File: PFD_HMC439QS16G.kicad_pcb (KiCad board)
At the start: 2 copper layers, 60.5 x 40.4 mm, 47 parts, among them J1 REF, J2 IN, J3 Out, J4 Supply, U1 HMC439QS16G, U2 LT3045EMSE, U3 LT3094EMSE, U4 ADA4896-2ARMZ

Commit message: Rev 1.1
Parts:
- removed REF** (x4): MountingHole_2.7mm_M2.5, Mounting_Holes:MountingHole_2.7mm_M2.5
- removed REF***: OSHW-Logo_5.7x6mm_SilkScreen, Symbols:OSHW-Logo_5.7x6mm_SilkScreen
- added C20: 560p, Capacitor_SMD:C_0603_1608Metric, F.Cu at (152.2, 100.8)
- added C21: 100n, Capacitor_SMD:C_0603_1608Metric, F.Cu at (136.8, 108.8)
- added C22: 100n, Capacitor_SMD:C_0603_1608Metric, F.Cu at (129.8, 114.8)
- added C23: 33p, Capacitor_SMD:C_0603_1608Metric, F.Cu at (125.2, 110.8)
- added C24: 330p, Capacitor_SMD:C_0603_1608Metric, F.Cu at (119.4, 106.1)
- added H1: MountingHole_Pad, MountingHole:MountingHole_4.3mm_M4_Pad_Via, F.Cu at (109.4, 73.5)
- added H2: MountingHole_Pad, MountingHole:MountingHole_4.3mm_M4_Pad_Via, F.Cu at (187.7, 73.5)
- added H3: MountingHole_Pad, MountingHole:MountingHole_4.3mm_M4_Pad_Via, F.Cu at (187.4, 121.6)
- added H4: MountingHole_Pad, MountingHole:MountingHole_4.3mm_M4_Pad_Via, F.Cu at (109.4, 121.5)
- added J5: JFET/Bias-T, Connector_Coaxial:SMA_Amphenol_901-144_Vertical, F.Cu at (111.8, 106.9)
- added JP1: Inverting, Jumper:SolderJumper-2_P1.3mm_Open_RoundedPad1.0x1.5mm, F.Cu at (129.9, 107.0)
- added JP2: Non-Inverting, Jumper:SolderJumper-2_P1.3mm_Open_RoundedPad1.0x1.5mm, F.Cu at (123.0, 109.5)
- added LOGO1: Logo_APQ, footprints:APQ-Logo, F.Cu at (143.0, 72.8)
- added LOGO2: Logo_Open_Hardware_Small, Symbol:OSHW-Logo_5.7x6mm_SilkScreen, B.Cu at (152.0, 118.8)
- added LOGO3: Logo_ROHS, Symbol:RoHS-Logo_6mm_SilkScreen, B.Cu at (169.0, 119.2)
- added R16: 200, Resistor_SMD:R_0603_1608Metric, F.Cu at (145.8, 121.0)
- added R17: 200, Resistor_SMD:R_0603_1608Metric, F.Cu at (134.0, 114.2)
- added R18: 200, Resistor_SMD:R_0603_1608Metric, F.Cu at (127.5, 110.8)
- added R19: 51, Resistor_SMD:R_1210_3225Metric, F.Cu at (126.2, 105.5)
- added R20: 1.2k, Resistor_SMD:R_0603_1608Metric, F.Cu at (122.1, 106.9)
- added R21: 51, Resistor_SMD:R_0603_1608Metric, F.Cu at (117.5, 106.1)
- added RV1: 1k, Potentiometer_THT:Potentiometer_Vishay_43_Horizontal, F.Cu at (142.2, 108.2)
- added U5: ADA4896-2ARMZ, footprints:MSOP-8_3x3mm_P0.65mm_mod, F.Cu at (132.2, 111.0)
- C1, C2: footprint Capacitors_SMD:C_0402 -> Capacitor_SMD:C_0402_1005Metric
- C10, C15, C16, C17, C18, C19, C5, C6, C9: footprint Capacitors_SMD:C_0603 -> Capacitor_SMD:C_0603_1608Metric
- C11, C12, C3, C4: footprint Capacitors_SMD:C_1210 -> Capacitor_SMD:C_1210_3225Metric
- C13, C14: value 200p -> 33p; footprint Capacitors_SMD:C_0603 -> Capacitor_SMD:C_0603_1608Metric
- C7: footprint Capacitors_SMD:C_1206 -> Capacitor_SMD:C_1206_3216Metric
- C8: value 4.7u -> 0.47u; footprint Capacitors_SMD:C_1206 -> Capacitor_SMD:C_1206_3216Metric
- J1, J2: footprint Connectors:SMA_THT_Jack_Straight -> Connector_Coaxial:SMA_Amphenol_901-144_Vertical
- J3: value Out -> Error_Out; footprint Connectors:SMA_THT_Jack_Straight -> Connector_Coaxial:SMA_Amphenol_901-144_Vertical
- J4: footprint Pin_Headers:Pin_Header_Straight_1x03_Pitch2.54mm -> Connector_PinHeader_2.54mm:PinHeader_1x03_P2.54mm_Vertical
- R1, R10, R11, R12, R13, R14, R2, R3, R4, R5, R6, R7, R8, R9: footprint Resistors_SMD:R_0603 -> Resistor_SMD:R_0603_1608Metric
- R15: footprint Resistors_SMD:R_1210 -> Resistor_SMD:R_1210_3225Metric
- U1: footprint custom:QSOP-16_EP_3.9x4.9mm_Pitch0.635mm -> footprints:QSOP-16_3.9x4.9mm_P0.635mm_EP_2.3mmx1.75mm
- U2, U3: footprint Housings_SSOP:MSOP-12-1EP_3x4mm_Pitch0.65mm -> Package_SO:MSOP-12-1EP_3x4mm_P0.65mm_EP1.65x2.85mm
- U4: footprint Housings_SSOP:MSOP-8_3x3mm_Pitch0.65mm -> footprints:MSOP-8_3x3mm_P0.65mm_mod
- moved C1 48.6 mm to (182.3, 106.9)
- moved J1 48.6 mm to (188.2, 106.9)
- moved C2 46.8 mm to (182.5, 91.8)
- moved J2 46.8 mm to (188.2, 91.8)
- moved R13 46.0 mm to (141.2, 98.8)
- moved C19 46.0 mm to (162.8, 106.4)
- moved C14 45.8 mm to (157.2, 94.7)
- moved C5 45.8 mm to (175.5, 100.0)
- moved C6 45.8 mm to (174.5, 95.4)
- moved R5 45.8 mm to (159.9, 96.3)
- moved R8 45.8 mm to (156.4, 102.4)
- moved U1 45.8 mm to (170.0, 99.7)
- moved C13 45.8 mm to (157.1, 104.8)
- moved R3 45.8 mm to (165.2, 94.2)
- moved R4 45.8 mm to (162.8, 103.2)
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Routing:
- net GND: track 254.2 -> 72.4 mm, vias 176 -> 237
- net IN: track 48.5 -> 14.5 mm, vias 9 -> 12
- net +5V: track 108.4 -> 140.9 mm
- net Net-(C16-Pad1): track 8.48 -> 36.4 mm, vias 0 -> 2
- net -5V: track 25.3 -> 43.9 mm
- net Net-(JP1-Pad1): track 0.00 -> 12.0 mm
- net Net-(C23-Pad2): track 0.00 -> 10.9 mm
- net Net-(C20-Pad1): track 10.0 -> 19.9 mm
- net Net-(C24-Pad1): track 0.00 -> 9.49 mm
- net Net-(RV1-Pad2): track 0.00 -> 8.91 mm
- net Net-(JP1-Pad2): track 0.00 -> 8.57 mm
- net Net-(C23-Pad1): track 0.00 -> 8.36 mm
- net Net-(C15-Pad1): track 6.74 -> 10.2 mm
- net Net-(C2-Pad1): track 8.97 -> 12.2 mm
- net Net-(C1-Pad1): track 8.82 -> 11.8 mm
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- added copper zone on B.Cu, net IN
- added copper zone on F.Cu, net IN
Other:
- board size 60.5 x 40.4 mm -> 108 x 58 mm
- board text added: "GND"
- board text added: "JFET/Bias-T non-inverting: JP1:open, JP2:closed, R17=R18 JFET/Bias-T inverting: JP1:closed, JP2:open, R17:DNF"
- board text added: "Phase-Frequency Detector 11/2020 Rev 1.1 Design: Tilman Preuschoff"
- board text removed: "Design: Tilman Preuschoff"
- board text removed: "Phase Frequency Detector 2019/02 Rev. 1.0"

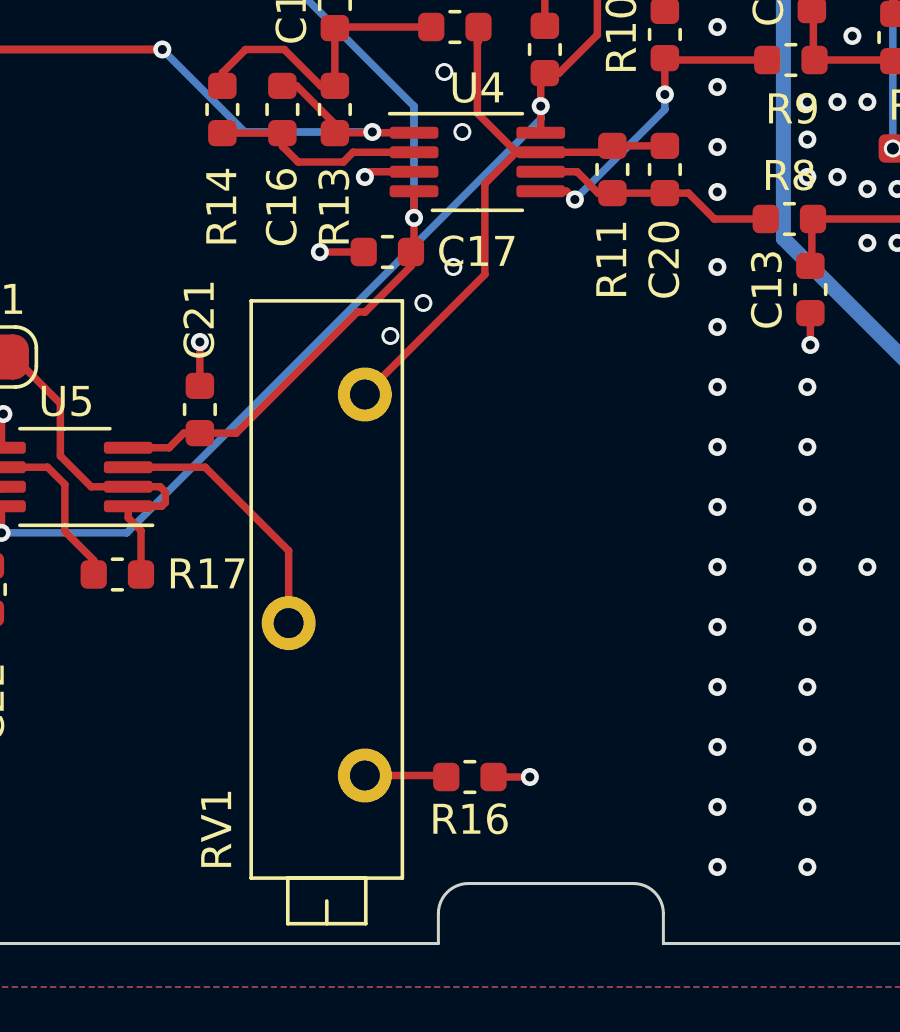
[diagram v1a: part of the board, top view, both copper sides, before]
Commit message: Reverse Trimpot. Update gerber files
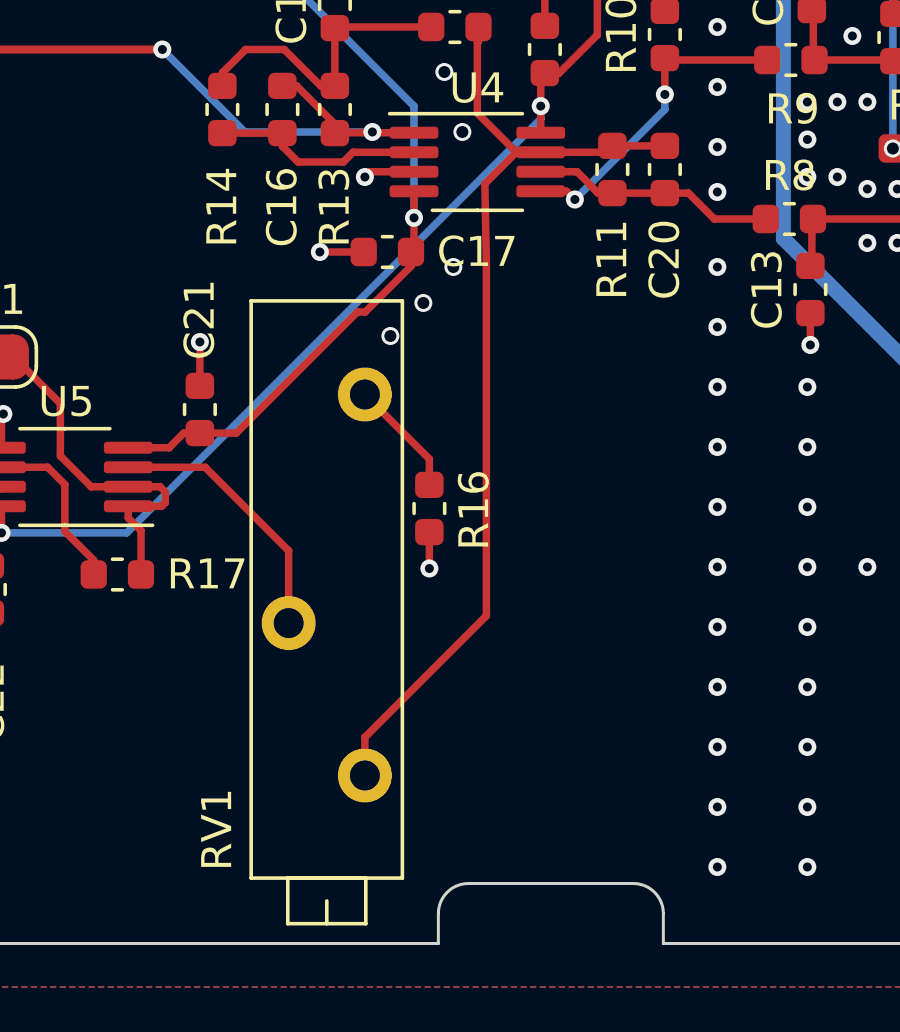
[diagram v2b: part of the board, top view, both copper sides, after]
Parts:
- moved R16 9.05 mm to (144.4, 112.0), turned to 90 degrees
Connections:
- RV1 pad 1: Net-(C20-Pad1) -> Net-(R16-Pad2)
- RV1 pad 3: Net-(R16-Pad2) -> Net-(C20-Pad1)
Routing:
- net Net-(C20-Pad1): track 19.9 -> 32.7 mm
- net Net-(R16-Pad2): track 2.73 -> 3.97 mm
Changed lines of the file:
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@@
     (thickness 1.6)
     (drawings 136)
-    (tracks 625)
+    (tracks 628)
     (zones 0)
     (modules 65)
@@
   )
   (module Resistor_SMD:R_0603_1608Metric (layer F.Cu)
-    (at 145.75 121 180)
+    (at 144.4 112.05 90)
     (descr "Resistor SMD 0603 (1608 Metric), square (rectangular) end terminal, IPC_7351 nominal, (Body size source: http://www.tortai-tech.com/upload/download/2011102023233369053.pdf), generated with kicad-footprint-generator")
     (tags resistor)
     (attr smd)
-    (fp_text reference R16 (at 0 -1.43) (layer F.SilkS)
+    (fp_text reference R16 (at -0.05 1.5 90) (layer F.SilkS)
       (effects (font (size 1 1) (thickness 0.15)))
     )
-    (fp_text value 200 (at 0 1.43) (layer F.Fab)
+    (fp_text value 200 (at 0 1.43 90) (layer F.Fab)
       (effects (font (size 1 1) (thickness 0.15)))
     )
@@
     (fp_line (start 1.48 -0.73) (end 1.48 0.73) (layer F.CrtYd) (width 0.05))
     (fp_line (start 1.48 0.73) (end -1.48 0.73) (layer F.CrtYd) (width 0.05))
-    (fp_text user %R (at 0 0) (layer F.Fab)
+    (fp_text user %R (at 0 0 90) (layer F.Fab)
       (effects (font (size 0.4 0.4) (thickness 0.06)))
     )
-    (pad 1 smd roundrect (at -0.7875 0 180) (size 0.875 0.95) (layers F.Cu F.Paste F.Mask) (roundrect_rratio 0.25)
+    (pad 1 smd roundrect (at -0.7875 0 90) (size 0.875 0.95) (layers F.Cu F.Paste F.Mask) (roundrect_rratio 0.25)
       (net 5 GND))
-    (pad 2 smd roundrect (at 0.7875 0 180) (size 0.875 0.95) (layers F.Cu F.Paste F.Mask) (roundrect_rratio 0.25)
+    (pad 2 smd roundrect (at 0.7875 0 90) (size 0.875 0.95) (layers F.Cu F.Paste F.Mask) (roundrect_rratio 0.25)
       (net 36 "Net-(R16-Pad2)"))
     (model ${KISYS3DMOD}/Resistor_SMD.3dshapes/R_0603_1608Metric.wrl
@@
     )
     (pad 1 thru_hole circle (at 0 0 90) (size 1.8 1.8) (drill 1) (layers *.Cu *.Mask)
-      (net 28 "Net-(C20-Pad1)"))
+      (net 36 "Net-(R16-Pad2)"))
     (pad 2 thru_hole circle (at -7.62 -2.54 90) (size 1.8 1.8) (drill 1) (layers *.Cu *.Mask)
       (net 37 "Net-(RV1-Pad2)"))
     (pad 3 thru_hole circle (at -12.7 0 90) (size 1.8 1.8) (drill 1) (layers *.Cu *.Mask)
-      (net 36 "Net-(R16-Pad2)"))
+      (net 28 "Net-(C20-Pad1)"))
     (model ${KISYS3DMOD}/Potentiometer_THT.3dshapes/Potentiometer_Vishay_43_Horizontal.wrl
       (at (xyz 0 0 0))
@@
   (gr_line (start 122.4 69.55) (end 116.4 69.55) (layer Dwgs.User) (width 0.2))
   (dimension 108 (width 0.3) (layer Dwgs.User)
-    (gr_text "108,000 mm" (at 148.4 142.35) (layer Dwgs.User)
+    (gr_text "108,000 mm" (at 123.05 114.7 90) (layer Dwgs.User)
       (effects (font (size 1.5 1.5) (thickness 0.3)))
     )
-    (feature1 (pts (xy 94.4 113.55) (xy 94.4 140.836421)))
-    (feature2 (pts (xy 202.4 113.55) (xy 202.4 140.836421)))
-    (crossbar (pts (xy 202.4 140.25) (xy 94.4 140.25)))
-    (arrow1a (pts (xy 94.4 140.25) (xy 95.526504 139.663579)))
-    (arrow1b (pts (xy 94.4 140.25) (xy 95.526504 140.836421)))
-    (arrow2a (pts (xy 202.4 140.25) (xy 201.273496 139.663579)))
-    (arrow2b (pts (xy 202.4 140.25) (xy 201.273496 140.836421)))
+    (feature1 (pts (xy 151.85 60.7) (xy 124.563579 60.7)))
+    (feature2 (pts (xy 151.85 168.7) (xy 124.563579 168.7)))
+    (crossbar (pts (xy 125.15 168.7) (xy 125.15 60.7)))
+    (arrow1a (pts (xy 125.15 60.7) (xy 125.736421 61.826504)))
+    (arrow1b (pts (xy 125.15 60.7) (xy 124.563579 61.826504)))
+    (arrow2a (pts (xy 125.15 168.7) (xy 125.736421 167.573496)))
+    (arrow2b (pts (xy 125.15 168.7) (xy 124.563579 167.573496)))
   )
   (gr_line (start 116.4 69.55) (end 116.4 68.05) (layer Dwgs.User) (width 0.2))
@@
   (via (at 163 95.25) (size 0.6) (drill 0.3) (layers F.Cu B.Cu) (net 5))
   (via (at 164 95.25) (size 0.6) (drill 0.3) (layers F.Cu B.Cu) (net 5))
-  (via (at 147.75 121) (size 0.6) (drill 0.3) (layers F.Cu B.Cu) (net 5))
-  (segment (start 146.5375 121) (end 147.75 121) (width 0.25) (layer F.Cu) (net 5))
+  (via (at 144.4 114.05) (size 0.6) (drill 0.3) (layers F.Cu B.Cu) (net 5))
+  (segment (start 144.4 112.8375) (end 144.4 114.05) (width 0.25) (layer F.Cu) (net 5))
   (via (at 130.2 108.9) (size 0.6) (drill 0.3) (layers F.Cu B.Cu) (net 5))
   (segment (start 130.1375 110.025) (end 130.1375 108.9625) (width 0.25) (layer F.Cu) (net 5))
@@
   (segment (start 146.0375 96) (end 146.0375 96.475) (width 0.25) (layer F.Cu) (net 28))
   (segment (start 146.0375 96.475) (end 146 96.5125) (width 0.25) (layer F.Cu) (net 28))
-  (segment (start 142.25 108.25) (end 146.25 104.25) (width 0.25) (layer F.Cu) (net 28))
   (segment (start 147.3 100.175) (end 148.1125 100.175) (width 0.25) (layer F.Cu) (net 28))
   (segment (start 146.25 101.225) (end 147.3 100.175) (width 0.25) (layer F.Cu) (net 28))
-  (segment (start 146.25 104.25) (end 146.25 101.225) (width 0.25) (layer F.Cu) (net 28))
-  (segment (start 125.75 106.9) (end 125.85 107) (width 0.25) (layer F.Cu) (net 38))
-  (segment (start 122.8875 106.9) (end 125.75 106.9) (width 0.25) (layer F.Cu) (net 38))
+  (segment (start 146.3 115.627208) (end 146.3 103.9) (width 0.25) (layer F.Cu) (net 28))
+  (segment (start 142.25 119.677208) (end 146.3 115.627208) (width 0.25) (layer F.Cu) (net 28))
+  (segment (start 142.25 120.95) (end 142.25 119.677208) (width 0.25) (layer F.Cu) (net 28))
+  (segment (start 146.3 103.9) (end 146.25 101.225) (width 0.25) (layer F.Cu) (net 28))
   (segment (start 125.25 111.5375) (end 127.5 111.5375) (width 0.25) (layer F.Cu) (net 29))
   (segment (start 128.1875 111.325) (end 129.325 111.325) (width 0.25) (layer F.Cu) (net 29))
@@
   (segment (start 130.1375 111.325) (end 130.1375 111.3875) (width 0.25) (layer F.Cu) (net 29))
   (segment (start 130.1375 111.3875) (end 130.14999 111.39999) (width 0.25) (layer F.Cu) (net 29))
-  (segment (start 122.8875 107.375) (end 122.8875 106.9) (width 0.25) (layer F.Cu) (net 38))
   (segment (start 125.25 111.5375) (end 124.775 111.5375) (width 0.25) (layer F.Cu) (net 29))
   (segment (start 124.3875 111.5375) (end 125.25 111.5375) (width 0.25) (layer F.Cu) (net 29))
@@
   (segment (start 135.475 111.975) (end 134.3625 111.975) (width 0.25) (layer F.Cu) (net 35))
   (segment (start 135.425 111.325) (end 135.6 111.5) (width 0.25) (layer F.Cu) (net 35))
-  (segment (start 144.9125 120.95) (end 144.9625 121) (width 0.25) (layer F.Cu) (net 36))
-  (segment (start 142.25 120.95) (end 144.9125 120.95) (width 0.25) (layer F.Cu) (net 36))
+  (segment (start 144.45 111.2125) (end 144.4 111.2625) (width 0.25) (layer F.Cu) (net 36))
+  (segment (start 144.4 110.4) (end 144.4 111.2625) (width 0.25) (layer F.Cu) (net 36))
+  (segment (start 142.25 108.25) (end 144.4 110.4) (width 0.25) (layer F.Cu) (net 36))
   (segment (start 134.3625 110.675) (end 136.925 110.675) (width 0.25) (layer F.Cu) (net 37))
   (segment (start 139.71 113.46) (end 139.71 115.87) (width 0.25) (layer F.Cu) (net 37))
   (segment (start 136.925 110.675) (end 139.71 113.46) (width 0.25) (layer F.Cu) (net 37))
+  (segment (start 125.75 106.9) (end 125.85 107) (width 0.25) (layer F.Cu) (net 38))
+  (segment (start 122.8875 106.9) (end 125.75 106.9) (width 0.25) (layer F.Cu) (net 38))
+  (segment (start 122.8875 107.375) (end 122.8875 106.9) (width 0.25) (layer F.Cu) (net 38))
   (segment (start 123 107.0125) (end 122.8875 106.9) (width 0.25) (layer F.Cu) (net 38))
   (segment (start 123 108.85) (end 123 107.0125) (width 0.25) (layer F.Cu) (net 38))
